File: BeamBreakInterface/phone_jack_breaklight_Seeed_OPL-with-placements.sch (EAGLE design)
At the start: 10 parts, among them J1 ST-PJ-312, J2 4P-SMD-2.0-90D, Q1 BSS138W-7-F

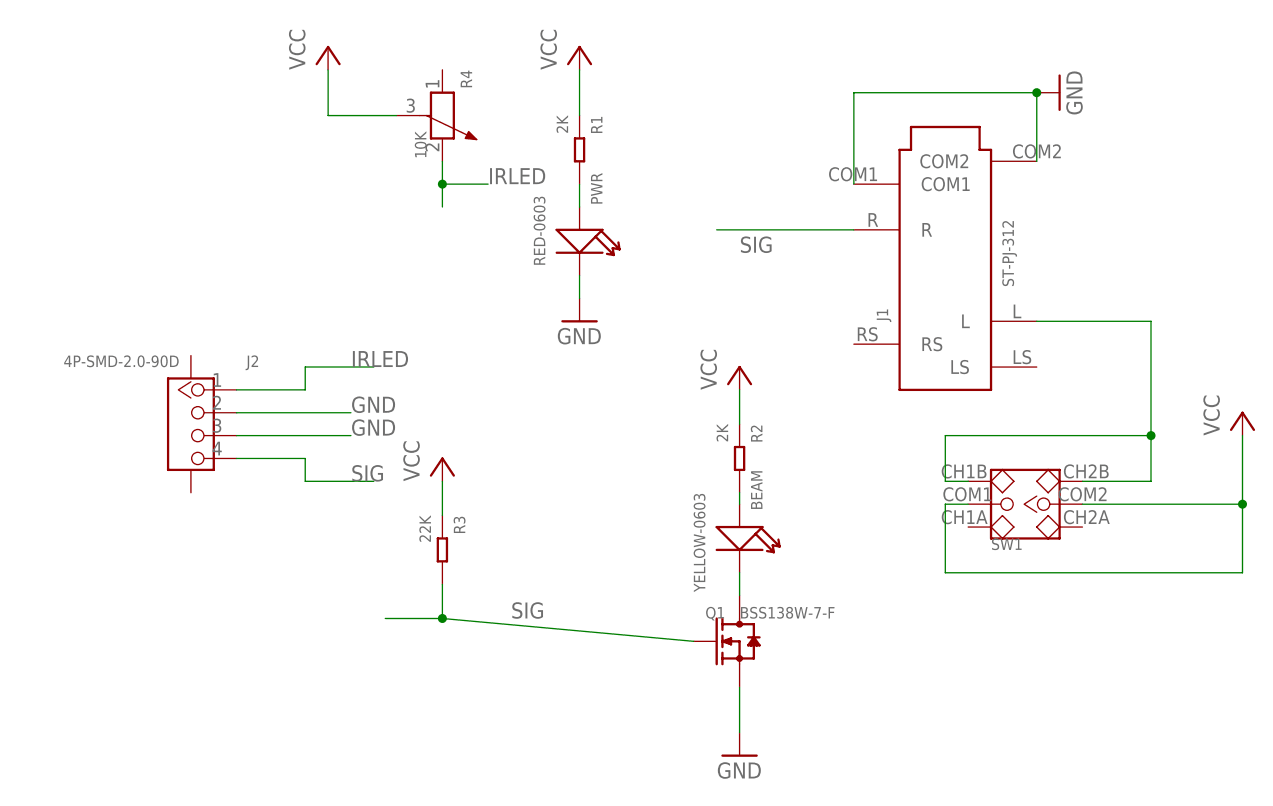
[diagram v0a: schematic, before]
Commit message: Updated design to fix error
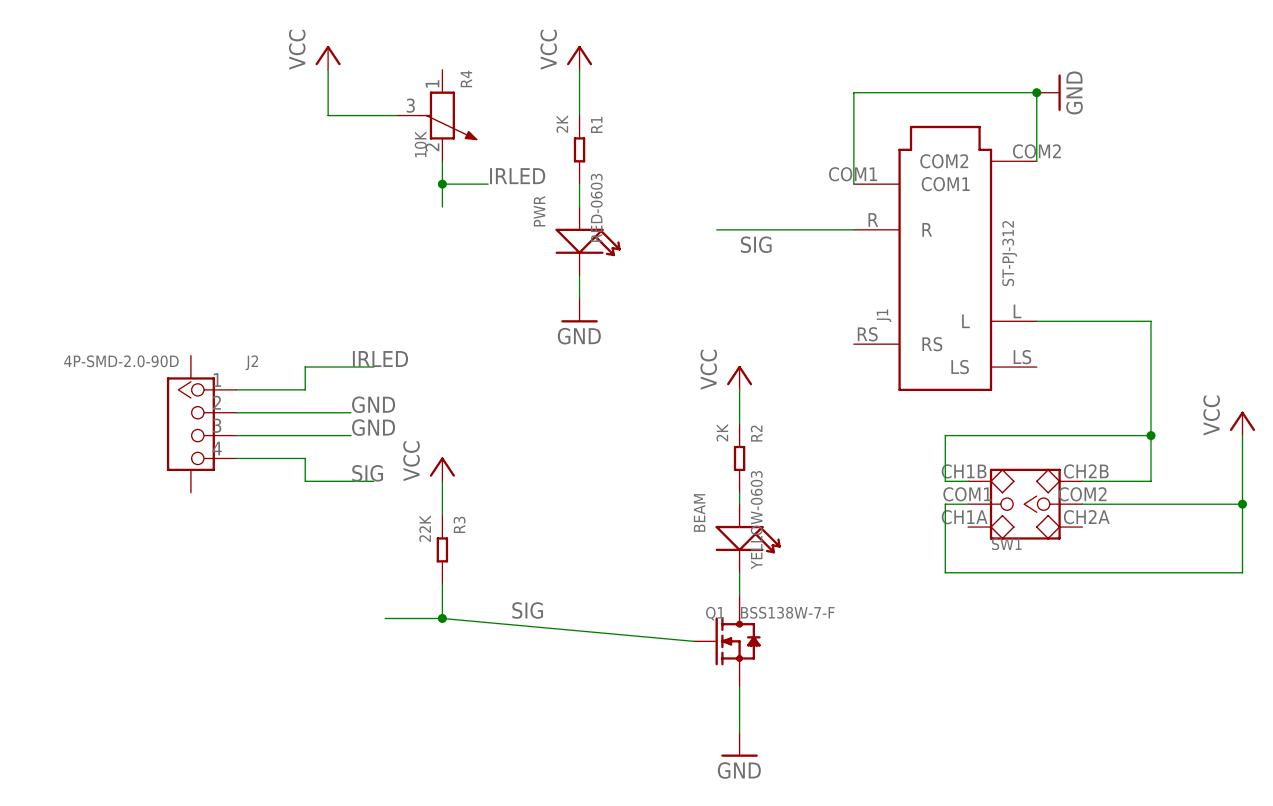
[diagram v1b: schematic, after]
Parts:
- RED-0603: value RED-0603 -> PWR
- YELLOW-0603: value YELLOW-0603 -> BEAM
- renumbered BEAM to YELLOW-0603, PWR to RED-0603
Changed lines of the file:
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@@
 <part name="P+1" library="supply1" deviceset="VCC" device=""/>
 <part name="J1" library="Seeed-Connector -2016" deviceset="AUDIO-JACK-6P-SMD(ST-PJ-312)" device="" value="ST-PJ-312"/>
-<part name="PWR" library="Seeed-LED-2016" deviceset="LED-SMD-RED-DIFFUSED(0603)" device="" value="RED-0603"/>
-<part name="BEAM" library="Seeed-LED-2016" deviceset="SMD-LED-CLEAR-YELLOW(0603)" device="" value="YELLOW-0603"/>
+<part name="RED-0603" library="Seeed-LED-2016" deviceset="LED-SMD-RED-DIFFUSED(0603)" device="" value="PWR"/>
+<part name="YELLOW-0603" library="Seeed-LED-2016" deviceset="SMD-LED-CLEAR-YELLOW(0603)" device="" value="BEAM"/>
 <part name="GND6" library="SparkFun" deviceset="GND" device=""/>
 <part name="Q1" library="Seeed-Transistor-2016" deviceset="SMD-MOSFET-N-CH-50V-200MA-BSS138W-7-F(SOT-23)" device="" value="BSS138W-7-F"/>
@@
 <instance part="P+1" gate="VCC" x="27.94" y="78.74"/>
 <instance part="J1" gate="G$1" x="68.58" y="54.61" rot="R90"/>
-<instance part="PWR" gate="G$1" x="27.94" y="57.15" rot="R270"/>
-<instance part="BEAM" gate="G$1" x="45.72" y="24.13" rot="R270"/>
+<instance part="RED-0603" gate="G$1" x="27.94" y="57.15" rot="R270"/>
+<instance part="YELLOW-0603" gate="G$1" x="45.72" y="24.13" rot="R270"/>
 <instance part="GND6" gate="1" x="81.28" y="73.66" rot="R90"/>
 <instance part="Q1" gate="G$1" x="45.72" y="12.7"/>
@@
 <segment>
 <pinref part="GND2" gate="1" pin="GND"/>
-<pinref part="PWR" gate="G$1" pin="-"/>
+<pinref part="RED-0603" gate="G$1" pin="-"/>
 <wire x1="27.94" y1="53.34" x2="27.94" y2="50.8" width="0.1524" layer="91"/>
 </segment>
@@
 <wire x1="45.72" y1="27.94" x2="45.72" y2="29.21" width="0.1524" layer="91"/>
 <pinref part="R2" gate="G$1" pin="2"/>
-<pinref part="BEAM" gate="G$1" pin="+"/>
+<pinref part="YELLOW-0603" gate="G$1" pin="+"/>
 </segment>
 </net>
@@
 <segment>
 <wire x1="45.72" y1="17.78" x2="45.72" y2="20.32" width="0.1524" layer="91"/>
-<pinref part="BEAM" gate="G$1" pin="-"/>
+<pinref part="YELLOW-0603" gate="G$1" pin="-"/>
 <pinref part="Q1" gate="G$1" pin="D"/>
 </segment>
@@
 <segment>
 <pinref part="R1" gate="G$1" pin="2"/>
-<pinref part="PWR" gate="G$1" pin="+"/>
+<pinref part="RED-0603" gate="G$1" pin="+"/>
 <wire x1="27.94" y1="60.96" x2="27.94" y2="63.5" width="0.1524" layer="91"/>
 </segment>
